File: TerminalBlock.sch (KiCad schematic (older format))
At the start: 0 parts

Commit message: associating-and-placing-the-terminal-atx-blocks
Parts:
- added K?: 3 Pin Terminal Block, symbol CONN_3
- added P?: 12 Pin Terminal Block, symbol CONN_12
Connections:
- net +3.3V: now also P?.2 (P2)
- net +5V: now also P?.1 (P1)
- net FAN_OUT+: now also P?.8 (P8)
- net FAN_OUT-: now also P?.9 (P9)
- net GND: now also P?.3 (P3)
- net LED_STRING+: now also P?.6 (P6)
- net LED_STRING-: now also P?.7 (P7)
- net RELAY_COM: now also K?.1 (P1)
- net RELAY_NC: now also K?.3 (P3)
- net RELAY_NO: now also K?.2 (PM)
- net TACH_IN: now also P?.10 (P10)
- net TC_IN+: now also P?.11 (P11)
- net V+_ADJ: now also P?.4 (P4)
- net V-_ADJ: now also P?.5 (P5)
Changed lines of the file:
@@
 $Descr A4 11693 8268
 encoding utf-8
-Sheet 7 9
+Sheet 5 9
 Title ""
 Date "23 feb 2014"
@@
 Comment4 ""
 $EndDescr
-Text HLabel 2750 2150 0    60   Input ~ 0
+Text HLabel 4750 3700 0    60   Input ~ 0
 V+_ADJ
-Text HLabel 2750 2300 0    60   Input ~ 0
+Text HLabel 4750 3850 0    60   Input ~ 0
 V-_ADJ
-Text HLabel 2750 2800 0    60   Output ~ 0
+Text HLabel 4750 4550 0    60   Output ~ 0
 FAN_OUT+
-Text HLabel 2750 3150 0    60   Input ~ 0
+Text HLabel 4750 4850 0    60   Input ~ 0
 TACH_IN
-Text HLabel 2750 2950 0    60   Output ~ 0
+Text HLabel 4750 4700 0    60   Output ~ 0
 FAN_OUT-
-Text HLabel 2700 3600 0    60   Output ~ 0
+Text HLabel 4750 4100 0    60   Output ~ 0
 LED_STRING+
-Text HLabel 2700 3800 0    60   Output ~ 0
+Text HLabel 4750 4250 0    60   Output ~ 0
 LED_STRING-
-Text HLabel 2750 4200 0    60   Input ~ 0
+Text HLabel 4750 5200 0    60   Input ~ 0
 TC_IN+
-Text HLabel 2750 4400 0    60   Input ~ 0
+Text HLabel 4750 5350 0    60   Input ~ 0
 TC_IN-
-Text HLabel 2750 6400 0    60   BiDi ~ 0
+Text HLabel 5500 1950 0    60   BiDi ~ 0
 RELAY_COM
-Text HLabel 2750 6600 0    60   BiDi ~ 0
+Text HLabel 5500 2150 0    60   BiDi ~ 0
 RELAY_NO
-Text HLabel 2750 6800 0    60   BiDi ~ 0
+Text HLabel 5500 2350 0    60   BiDi ~ 0
 RELAY_NC
 $Comp
 L +5V #PWR020
 U 1 1 52F5D989
-P 2750 1300
-F 0 "#PWR020" H 2750 1390 20  0001 C CNN
-F 1 "+5V" H 2750 1390 30  0000 C CNN
-F 2 "" H 2750 1300 60  0000 C CNN
-F 3 "" H 2750 1300 60  0000 C CNN
-	1    2750 1300
-	1    0    0    -1
+P 4700 3100
+F 0 "#PWR020" H 4700 3190 20  0001 C CNN
+F 1 "+5V" H 4700 3190 30  0000 C CNN
+F 2 "" H 4700 3100 60  0000 C CNN
+F 3 "" H 4700 3100 60  0000 C CNN
+	1    4700 3100
+	0    -1   -1   0
 $EndComp
 $Comp
 L +3.3V #PWR021
 U 1 1 52F5D998
-P 2750 1500
-F 0 "#PWR021" H 2750 1460 30  0001 C CNN
-F 1 "+3.3V" H 2750 1610 30  0000 C CNN
-F 2 "" H 2750 1500 60  0000 C CNN
-F 3 "" H 2750 1500 60  0000 C CNN
-	1    2750 1500
-	1    0    0    -1
+P 4700 3250
+F 0 "#PWR021" H 4700 3210 30  0001 C CNN
+F 1 "+3.3V" H 4700 3360 30  0000 C CNN
+F 2 "" H 4700 3250 60  0000 C CNN
+F 3 "" H 4700 3250 60  0000 C CNN
+	1    4700 3250
+	0    -1   -1   0
 $EndComp
 $Comp
 L GND #PWR022
 U 1 1 52F5D9A7
-P 2750 1700
-F 0 "#PWR022" H 2750 1700 30  0001 C CNN
-F 1 "GND" H 2750 1630 30  0001 C CNN
-F 2 "" H 2750 1700 60  0000 C CNN
-F 3 "" H 2750 1700 60  0000 C CNN
-	1    2750 1700
+P 4700 3400
+F 0 "#PWR022" H 4700 3400 30  0001 C CNN
+F 1 "GND" H 4700 3330 30  0001 C CNN
+F 2 "" H 4700 3400 60  0000 C CNN
+F 3 "" H 4700 3400 60  0000 C CNN
+	1    4700 3400
+	0    1    1    0
+$EndComp
+$Comp
+L CONN_3 K?
+U 1 1 530A7290
+P 6050 2150
+F 0 "K?" V 6000 2150 50  0000 C CNN
+F 1 "3 Pin Terminal Block" V 6100 2150 40  0000 C CNN
+F 2 "" H 6050 2150 60  0000 C CNN
+F 3 "http://media.digikey.com/pdf/Data%20Sheets/Phoenix%20Contact%20PDFs/COMBICON%20Compact%205.0mm%20Series.pdf" H 6050 2150 60  0001 C CNN
+F 4 "Phoenix Contact" H 6050 2150 60  0001 C CNN "MFG Name"
+F 5 "1935174" H 6050 2150 60  0001 C CNN "MFG Part Number"
+F 6 "DigiKey" H 6050 2150 60  0001 C CNN "Distributor"
+F 7 "277-1578-ND" H 6050 2150 60  0001 C CNN "Distributor Part Number"
+F 8 "http://www.digikey.com/product-detail/en/1935174/277-1578-ND/568615" H 6050 2150 60  0001 C CNN "Distributor Link"
+	1    6050 2150
 	1    0    0    -1
 $EndComp
+$Comp
+L CONN_12 P?
+U 1 1 530A7609
+P 6650 4300
+F 0 "P?" V 6600 4300 60  0000 C CNN
+F 1 "12 Pin Terminal Block" V 6700 4300 60  0000 C CNN
+F 2 "" H 6650 4300 60  0000 C CNN
+F 3 "" H 6650 4300 60  0000 C CNN
+F 4 "On Shore" H 6650 4300 60  0001 C CNN "MFG Name"
+F 5 "OSTTE120104" H 6650 4300 60  0001 C CNN "MFG Part Number"
+F 6 "Digikey" H 6650 4300 60  0001 C CNN "Distributor"
+F 7 "ED2737-ND" H 6650 4300 60  0001 C CNN "Distributor Part Number"
+F 8 "http://www.digikey.com/product-detail/en/OSTTE120104/ED2737-ND/2351813" H 6650 4300 60  0001 C CNN "Distributor Link"
+	1    6650 4300
+	1    0    0    -1
+$EndComp
+Wire Wire Line
+	4700 3100 6100 3100
+Wire Wire Line
+	6100 3100 6100 3750
+Wire Wire Line
+	6100 3750 6300 3750
+Wire Wire Line
+	4700 3250 6000 3250
+Wire Wire Line
+	6000 3250 6000 3850
+Wire Wire Line
+	6000 3850 6300 3850
+Wire Wire Line
+	4700 3400 5900 3400
+Wire Wire Line
+	5900 3400 5900 3950
+Wire Wire Line
+	5900 3950 6300 3950
+Wire Wire Line
+	4750 3700 5800 3700
+Wire Wire Line
+	5800 3700 5800 4050
+Wire Wire Line
+	5800 4050 6300 4050
+Wire Wire Line
+	4750 3850 5700 3850
+Wire Wire Line
+	5700 3850 5700 4150
+Wire Wire Line
+	5700 4150 6300 4150
+Wire Wire Line
+	4750 4100 5600 4100
+Wire Wire Line
+	5600 4100 5600 4250
+Wire Wire Line
+	5600 4250 6300 4250
+Wire Wire Line
+	4750 4250 5500 4250
+Wire Wire Line
+	5500 4250 5500 4350
+Wire Wire Line
+	5500 4350 6300 4350
+Wire Wire Line
+	4750 4550 5500 4550
+Wire Wire Line
+	5500 4550 5500 4450
+Wire Wire Line
+	5500 4450 6300 4450
+Wire Wire Line
+	4750 4700 5600 4700
+Wire Wire Line
+	5600 4700 5600 4550
+Wire Wire Line
+	5600 4550 6300 4550
+Wire Wire Line
+	4750 4850 5700 4850
+Wire Wire Line
+	5700 4850 5700 4650
+Wire Wire Line
+	5700 4650 6300 4650
+Wire Wire Line
+	4750 5200 5800 5200
+Wire Wire Line
+	5800 5200 5800 4750
+Wire Wire Line
+	5800 4750 6300 4750
+Wire Wire Line
+	4800 5350 5900 5350
+Wire Wire Line
+	5900 5350 5900 4850
+Wire Wire Line
+	5900 4850 6300 4850
+Wire Wire Line
+	5500 1950 5600 1950
+Wire Wire Line
+	5600 1950 5600 2050
+Wire Wire Line
+	5600 2050 5700 2050
+Wire Wire Line
+	5500 2150 5700 2150
+Wire Wire Line
+	5500 2350 5600 2350
+Wire Wire Line
+	5600 2350 5600 2250
+Wire Wire Line
+	5600 2250 5700 2250
 $EndSCHEMATC

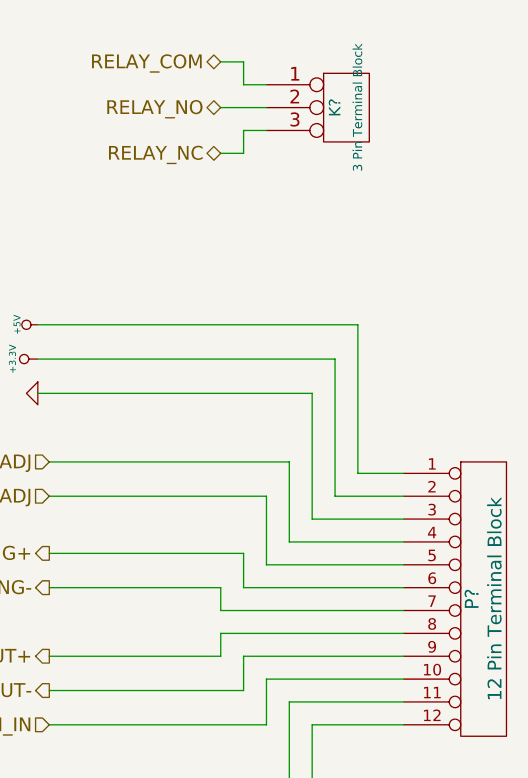
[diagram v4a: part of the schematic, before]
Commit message: associating-and-placing-the-terminalatx-blocks
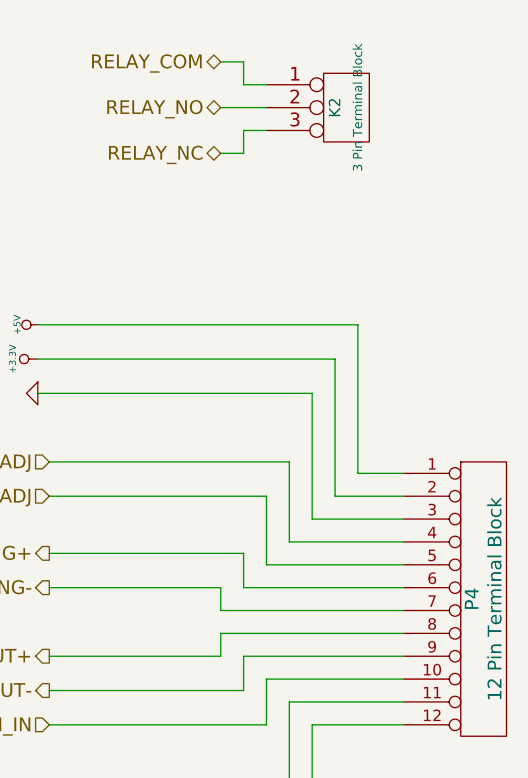
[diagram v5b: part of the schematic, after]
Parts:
- gave numbers to parts that had none: 2
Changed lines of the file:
@@
 RELAY_NC
 $Comp
-L +5V #PWR020
+L +5V #PWR20
 U 1 1 52F5D989
 P 4700 3100
-F 0 "#PWR020" H 4700 3190 20  0001 C CNN
+F 0 "#PWR20" H 4700 3190 20  0001 C CNN
 F 1 "+5V" H 4700 3190 30  0000 C CNN
 F 2 "" H 4700 3100 60  0000 C CNN
@@
 $EndComp
 $Comp
-L +3.3V #PWR021
+L +3.3V #PWR21
 U 1 1 52F5D998
 P 4700 3250
-F 0 "#PWR021" H 4700 3210 30  0001 C CNN
+F 0 "#PWR21" H 4700 3210 30  0001 C CNN
 F 1 "+3.3V" H 4700 3360 30  0000 C CNN
 F 2 "" H 4700 3250 60  0000 C CNN
@@
 $EndComp
 $Comp
-L GND #PWR022
+L GND #PWR22
 U 1 1 52F5D9A7
 P 4700 3400
-F 0 "#PWR022" H 4700 3400 30  0001 C CNN
+F 0 "#PWR22" H 4700 3400 30  0001 C CNN
 F 1 "GND" H 4700 3330 30  0001 C CNN
 F 2 "" H 4700 3400 60  0000 C CNN
@@
 $EndComp
 $Comp
-L CONN_3 K?
+L CONN_3 K2
 U 1 1 530A7290
 P 6050 2150
-F 0 "K?" V 6000 2150 50  0000 C CNN
+F 0 "K2" V 6000 2150 50  0000 C CNN
 F 1 "3 Pin Terminal Block" V 6100 2150 40  0000 C CNN
 F 2 "" H 6050 2150 60  0000 C CNN
@@
 $EndComp
 $Comp
-L CONN_12 P?
+L CONN_12 P4
 U 1 1 530A7609
 P 6650 4300
-F 0 "P?" V 6600 4300 60  0000 C CNN
+F 0 "P4" V 6600 4300 60  0000 C CNN
 F 1 "12 Pin Terminal Block" V 6700 4300 60  0000 C CNN
 F 2 "" H 6650 4300 60  0000 C CNN
